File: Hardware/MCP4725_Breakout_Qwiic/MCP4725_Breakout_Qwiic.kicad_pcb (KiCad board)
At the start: 2 copper layers, 25.4 x 25.4 mm, 50 parts, among them J1 Conn_01x02, J2 I2C, J3 Qwiic_RA, J4 Qwiic_RA, U2 MCP4725

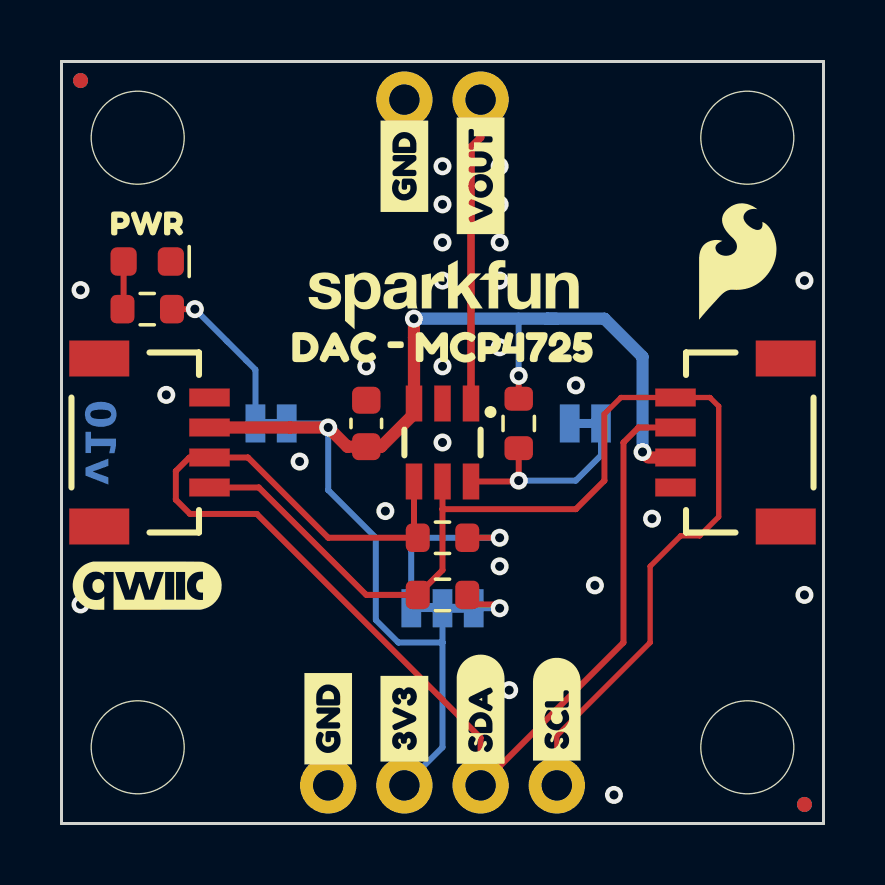
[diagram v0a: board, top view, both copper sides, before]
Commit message: Puts PTH on one side
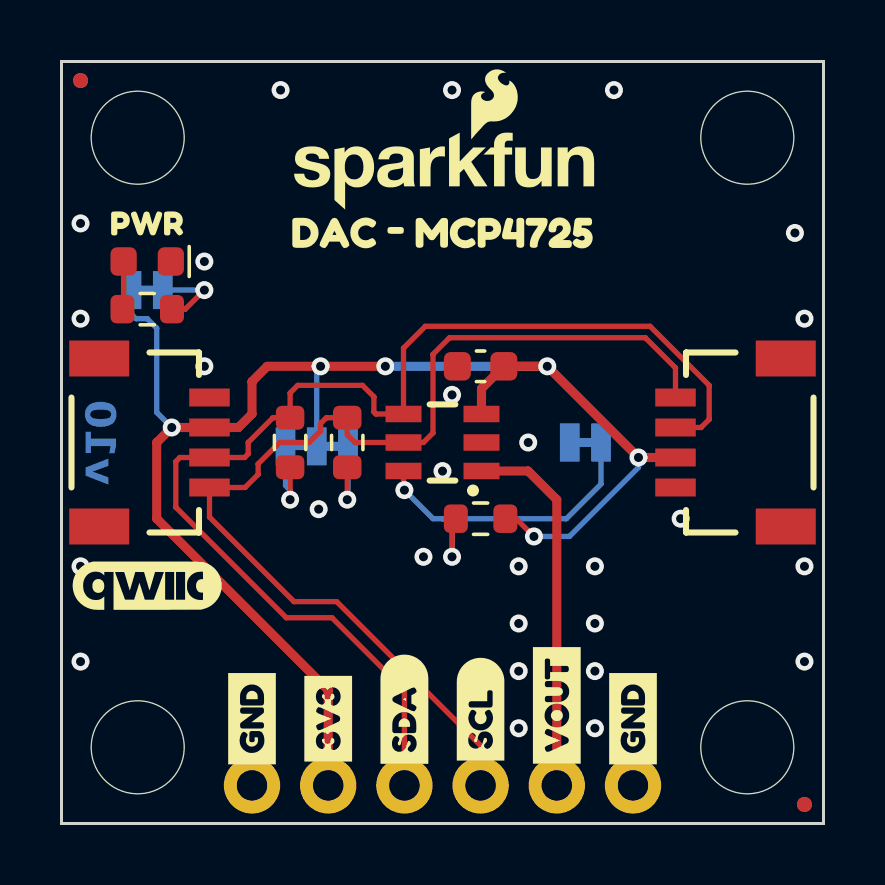
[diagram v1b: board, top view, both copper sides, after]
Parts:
- removed the G*** at (163.5, 93.7)
- removed the G*** at (153.7, 94.6)
- removed kibuzzard-69BC0559: G***, kibuzzard-69BC0559
- removed kibuzzard-69BC0561: G***, kibuzzard-69BC0561
- removed kibuzzard-69BC0567: G***, kibuzzard-69BC0567
- added G***: LOGO, SparkFun-Aesthetic:SparkFun_Logo_10mm, F.Cu at (153.7, 90.5)
- added kibuzzard-69C55E7A: G***, kibuzzard-69C55E7A, B.Cu at (146.3, 94.6)
- added kibuzzard-69C55E8E: G***, kibuzzard-69C55E8E, B.Cu at (152.3, 99.7)
- added kibuzzard-69C55EC8: G***, kibuzzard-69C55EC8, B.Cu at (161.3, 99.7)
- moved J1 23.0 mm to (157.5, 111.1), turned to 0 degrees
- moved kibuzzard-69B46D94 19.9 mm to (160.0, 108.9) (x2)
- moved kibuzzard-69B46D81 17.8 mm to (157.5, 108.5) (x2)
- moved JP1 6.83 mm to (149.5, 99.8)
- moved JP3 6.07 mm to (143.8, 94.6), turned to 180 degrees
- moved R5 5.99 mm to (150.5, 99.7), turned to -90 degrees
- moved R4 5.99 mm to (148.6, 99.7), turned to -90 degrees
- moved C1 4.26 mm to (154.9, 97.2), turned to 180 degrees
- moved kibuzzard-69BC0473 3.81 mm to (153.7, 92.7)
- moved R1 3.42 mm to (154.9, 102.2), turned to 0 degrees
- moved J2 2.54 mm to (147.3, 111.1)
- moved kibuzzard-69B46D94 2.54 mm to (147.3, 108.9) (x2)
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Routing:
- net 3.3V: track 43.4 -> 51.4 mm, vias 4 -> 6
- net ADDR: track 6.84 -> 12.4 mm, vias 1 -> 2
- net SCL: track 40.0 -> 36.4 mm
- net Net-(JP1-C): track 6.14 -> 2.92 mm
- net Net-(JP3-A): track 5.41 -> 2.73 mm
- net VOUT: track 10.3 -> 12.4 mm
- net SDA: track 42.6 -> 40.8 mm
- net Net-(JP1-A): track 2.13 -> 2.87 mm
- net GND: vias 25 -> 27

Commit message: Adds measures, grows small board by another 1/8 inch in X/Y direction
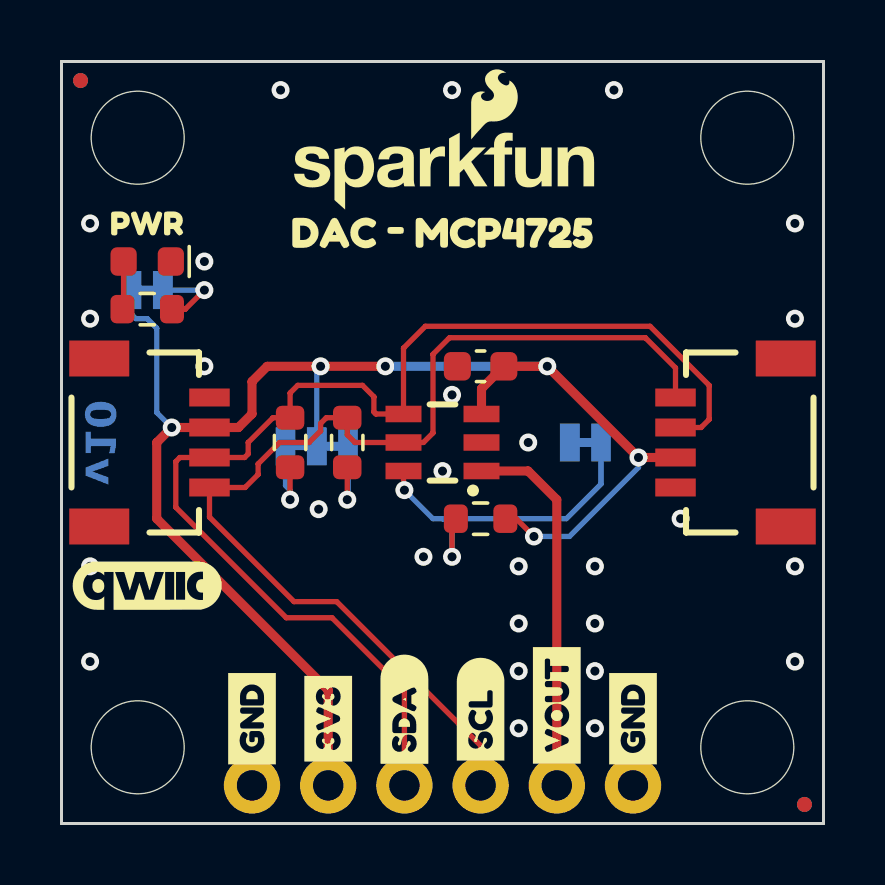
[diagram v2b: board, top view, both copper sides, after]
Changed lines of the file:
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@@
 				(font
 					(size 0.001 0.001)
+					(thickness 0.15)
 				)
 				(justify mirror)
@@
 				(font
 					(size 0.001 0.001)
+					(thickness 0.15)
 				)
 				(justify mirror)
@@
 				(font
 					(size 0.001 0.001)
+					(thickness 0.15)
 				)
 				(justify mirror)
@@
 				(font
 					(size 0.001 0.001)
+					(thickness 0.15)
 				)
 				(justify mirror)
@@
 				(font
 					(size 0.001 0.001)
+					(thickness 0.15)
 				)
 				(justify mirror)
@@
 				(font
 					(size 0.001 0.001)
+					(thickness 0.15)
 				)
 				(justify mirror)
@@
 	(dimension
 		(type orthogonal)
-		(layer "User.1")
+		(layer "Dwgs.User")
 		(pts
 			(xy 143.3195 89.535) (xy 143.3195 86.995)
@@
 		(gr_text "0.1"
 			(at 134.486 88.265 90)
-			(layer "User.1")
+			(layer "Dwgs.User")
 			(effects
 				(font
@@
 	(dimension
 		(type orthogonal)
-		(layer "User.1")
+		(layer "Dwgs.User")
 		(pts
 			(xy 152.4 88.265) (xy 140.97 88.38)
@@
 		(gr_text "0.45"
 			(at 146.685 80.892 0)
-			(layer "User.1")
+			(layer "Dwgs.User")
 			(effects
 				(font
@@
 	(dimension
 		(type orthogonal)
-		(layer "User.1")
+		(layer "Dwgs.User")
 		(pts
 			(xy 166.37 112.395) (xy 161.4375 99.695)
@@
 		(gr_text "0.5"
 			(at 172.205 106.045 90)
-			(layer "User.1")
+			(layer "Dwgs.User")
 			(effects
 				(font
@@
 	(dimension
 		(type orthogonal)
-		(layer "User.1")
+		(layer "Dwgs.User")
 		(pts
 			(xy 153.67 99.695) (xy 140.97 99.695)
@@
 		(gr_text "0.5"
 			(at 147.32 123.818 0)
-			(layer "User.1")
+			(layer "Dwgs.User")
 			(effects
 				(font
@@
 	(dimension
 		(type orthogonal)
-		(layer "User.1")
+		(layer "Dwgs.User")
 		(pts
 			(xy 143.51 89.535) (xy 140.97 89.535)
@@
 		(gr_text "0.1"
 			(at 142.24 83.813 0)
-			(layer "User.1")
+			(layer "Dwgs.User")
 			(effects
 				(font
@@
 	(dimension
 		(type orthogonal)
-		(layer "User.1")
+		(layer "Dwgs.User")
 		(pts
 			(xy 143.51 89.535) (xy 143.51 109.855)
@@
 		(gr_text "0.8"
 			(at 134.486 99.695 90)
-			(layer "User.1")
+			(layer "Dwgs.User")
 			(effects
 				(font
@@
 	(dimension
 		(type orthogonal)
-		(layer "User.1")
+		(layer "Dwgs.User")
 		(pts
 			(xy 140.97 86.995) (xy 140.97 112.395)
@@
 		(gr_text "1"
 			(at 131.819 99.695 90)
-			(layer "User.1")
+			(layer "Dwgs.User")
 			(effects
 				(font
@@
 	(dimension
 		(type orthogonal)
-		(layer "User.1")
+		(layer "Dwgs.User")
 		(pts
 			(xy 140.97 86.995) (xy 166.37 86.995)
@@
 		(gr_text "1"
 			(at 153.67 78.225 0)
-			(layer "User.1")
+			(layer "Dwgs.User")
 			(effects
 				(font
@@
 	(dimension
 		(type orthogonal)
-		(layer "User.1")
+		(layer "Dwgs.User")
 		(pts
-			(xy 149.86 111.125) (xy 140.97 111.125)
+			(xy 147.32 111.125) (xy 140.97 111.125)
 		)
 		(height 8.509)
@@
 			(keep_text_aligned yes)
 		)
-		(gr_text "0.35"
-			(at 145.415 118.484 0)
-			(layer "User.1")
+		(gr_text "0.25"
+			(at 144.145 118.484 0)
+			(layer "Dwgs.User")
 			(effects
 				(font
@@
 	)
 	(via
-		(at 165.735 103.8225)
+		(at 165.4175 103.8225)
 		(size 0.6)
 		(drill 0.3)
@@
 	)
 	(via
-		(at 141.605 103.8225)
+		(at 141.9225 103.8225)
 		(size 0.6)
 		(drill 0.3)
@@
 	)
 	(via
-		(at 141.605 95.5675)
+		(at 141.9225 95.5675)
 		(size 0.6)
 		(drill 0.3)
@@
 	)
 	(via
-		(at 141.605 106.9975)
+		(at 141.9225 106.9975)
 		(size 0.6)
 		(drill 0.3)
@@
 	)
 	(via
-		(at 165.735 95.5675)
+		(at 165.4175 95.5675)
 		(size 0.6)
 		(drill 0.3)
@@
 	)
 	(via
-		(at 141.605 92.3925)
+		(at 141.9225 92.3925)
 		(size 0.6)
 		(drill 0.3)
@@
 	)
 	(via
-		(at 165.735 106.9975)
+		(at 165.4175 106.9975)
 		(size 0.6)
 		(drill 0.3)
@@
 	)
 	(via
-		(at 165.4175 92.71)
+		(at 165.4175 92.3925)
 		(size 0.6)
 		(drill 0.3)
